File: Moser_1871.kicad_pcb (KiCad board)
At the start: 2 copper layers, 39 x 115 mm, 35 parts, among them Q14 3B SENSE / PINOUT VERIFY, SW1 SLIDE CONTACT / APPROX, U1 ATTINY461V-10SU

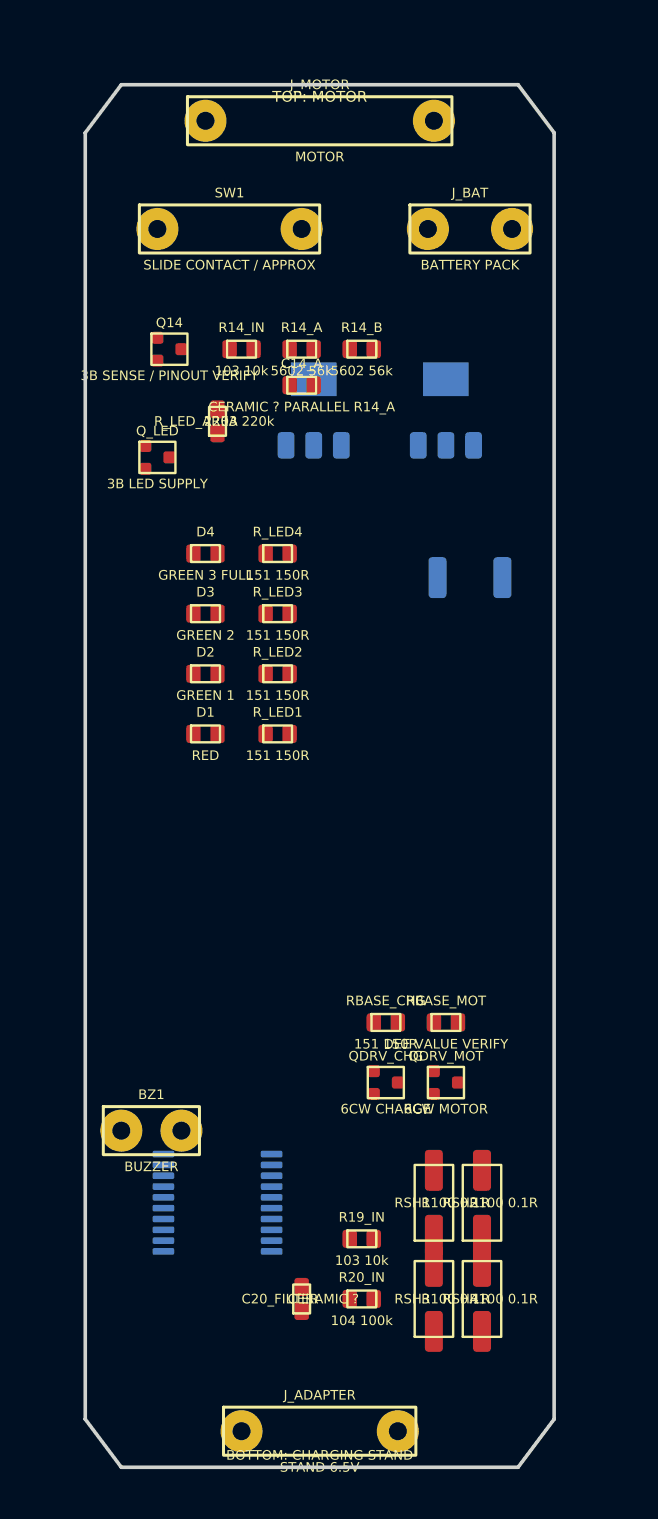
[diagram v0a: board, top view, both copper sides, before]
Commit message: Expand PCB component and via placement from board photos
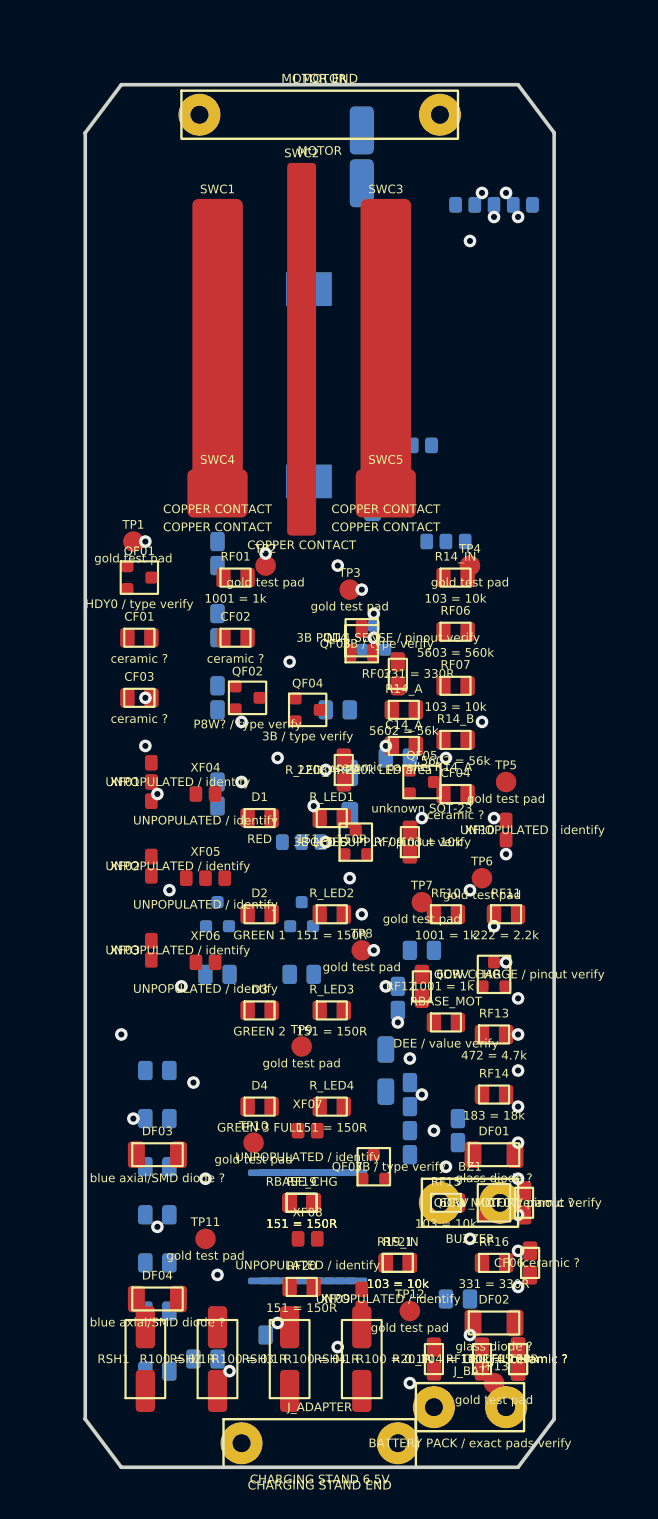
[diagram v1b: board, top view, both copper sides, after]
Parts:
- removed the D_MOTOR at (130.0, 91.0)
- removed the Q_CHG at (117.0, 77.0)
- removed the Q_MOT at (128.0, 77.0)
- removed SW1: SLIDE CONTACT / APPROX, Moser_RE:TH_2P
- added CB01: ceramic ?, Moser_RE:0805_2P, B.Cu at (104.0, 152.0)
- added CB02: ceramic ?, Moser_RE:0805_2P, B.Cu at (104.0, 148.0)
- added CB03: ceramic ?, Moser_RE:0805_2P, B.Cu at (104.0, 144.0)
- added CB04: ceramic ?, Moser_RE:0805_2P, B.Cu at (104.0, 140.0)
- added CB05: ceramic ?, Moser_RE:0805_2P, B.Cu at (104.0, 136.0)
- added CB06: ceramic ?, Moser_RE:0805_2P, B.Cu at (104.0, 132.0)
- added CB07: ceramic MCU, Moser_RE:0805_2P, B.Cu at (125.0, 138.0)
- added CB08: ceramic ?, Moser_RE:0805_2P, B.Cu at (124.0, 106.0)
- added CB09: ceramic ?, Moser_RE:0805_2P, B.Cu at (126.0, 122.0)
- added CB10: ceramic ?, Moser_RE:0805_2P, B.Cu at (129.0, 137.0)
- added CB11: ceramic ?, Moser_RE:0805_2P, B.Cu at (114.0, 154.0)
- added CF01: ceramic ?, Moser_RE:0805_2P, F.Cu at (102.5, 96.0)
- added CF02: ceramic ?, Moser_RE:0805_2P, F.Cu at (110.5, 96.0)
- added CF03: ceramic ?, Moser_RE:0805_2P, F.Cu at (102.5, 101.0)
- added CF04: ceramic ?, Moser_RE:0805_2P, F.Cu at (128.8, 109.0)
- added CF05: ceramic ?, Moser_RE:0805_2P, F.Cu at (134.0, 156.0)
- added CF06: ceramic ?, Moser_RE:0805_2P, F.Cu at (135.0, 148.0)
- added CF07: ceramic ?, Moser_RE:0805_2P, F.Cu at (134.5, 143.0)
- added DB01: glass diode ?, Moser_RE:MELF_2P, B.Cu at (120.0, 109.0)
- added DB02: small diode ?, Moser_RE:MELF_2P, B.Cu at (123.0, 132.0)
- added DF01: glass diode ?, Moser_RE:MELF_2P, F.Cu at (132.0, 139.0)
- added DF02: glass diode ?, Moser_RE:MELF_2P, F.Cu at (132.0, 153.0)
- added DF03: blue axial/SMD diode ?, Moser_RE:MELF_2P, F.Cu at (104.0, 139.0)
- added DF04: blue axial/SMD diode ?, Moser_RE:MELF_2P, F.Cu at (104.0, 151.0)
- added D_MOTOR: SS24, Moser_RE:SMB_2P, B.Cu at (121.0, 56.0)
- added QB01: 6CW / type verify, Moser_RE:SOT-23, B.Cu at (109.0, 119.0)
- added QB02: 6CW / type verify, Moser_RE:SOT-23, B.Cu at (116.0, 119.0)
- added QB03: unknown transistor/diode, Moser_RE:SOT-23, B.Cu at (122.0, 96.0)
- added QF01: HDY0 / type verify, Moser_RE:SOT-23, F.Cu at (102.5, 91.0)
- added QF02: P8W? / type verify, Moser_RE:SOT-23, F.Cu at (111.5, 101.0)
- added QF03: 3B / type verify, Moser_RE:SOT-23, F.Cu at (121.0, 96.5)
- added QF04: 3B / type verify, Moser_RE:SOT-23, F.Cu at (116.5, 102.0)
- added QF05: unknown SOT-23, Moser_RE:SOT-23, F.Cu at (126.0, 108.0)
- added QF07: 3B / type verify, Moser_RE:SOT-23, F.Cu at (122.0, 140.0)
- added Q_CHG: FZT968 CHARGE, Moser_RE:SOT-223, B.Cu at (119.0, 83.0)
- added Q_MOT: FZT968 MOTOR, Moser_RE:SOT-223, B.Cu at (119.0, 67.0)
- added RB01: 103 = 10k, Moser_RE:0805_2P, B.Cu at (104.0, 157.0)
- added RB02: 103 = 10k, Moser_RE:0805_2P, B.Cu at (108.0, 156.0)
- added RB03: 104 = 100k, Moser_RE:0805_2P, B.Cu at (125.0, 134.0)
- added RB04: 101 = 100R, Moser_RE:0805_2P, B.Cu at (129.0, 151.0)
- added RB05: 1001 = 1k, Moser_RE:0805_2P, B.Cu at (109.0, 124.0)
- added RB06: 1001 = 1k, Moser_RE:0805_2P, B.Cu at (116.0, 124.0)
- added RB07: 151 = 150R, Moser_RE:0805_2P, B.Cu at (109.0, 109.0)
- added RB08: DEE / value verify, Moser_RE:0805_2P, B.Cu at (109.0, 101.0)
- added RB09: 561 = 560R, Moser_RE:0805_2P, B.Cu at (109.0, 95.0)
- added RB10: 103 = 10k, Moser_RE:0805_2P, B.Cu at (109.0, 89.0)
- added RB11: 1001 = 1k, Moser_RE:0805_2P, B.Cu at (119.0, 102.0)
- added RB12: 1001 = 1k, Moser_RE:0805_2P, B.Cu at (124.0, 126.0)
- added RF01: 1001 = 1k, Moser_RE:0805_2P, F.Cu at (110.5, 91.0)
- added RF02: 331 = 330R, Moser_RE:0805_2P, F.Cu at (124.0, 99.0)
- added RF06: 5603 = 560k, Moser_RE:0805_2P, F.Cu at (128.8, 95.5)
- added RF07: 103 = 10k, Moser_RE:0805_2P, F.Cu at (128.8, 100.0)
- added RF09: 103 = 10k, Moser_RE:0805_2P, F.Cu at (125.0, 113.0)
- added RF10: 1001 = 1k, Moser_RE:0805_2P, F.Cu at (128.0, 119.0)
- added RF11: 222 = 2.2k, Moser_RE:0805_2P, F.Cu at (133.0, 119.0)
- added RF12: 1001 = 1k, Moser_RE:0805_2P, F.Cu at (126.0, 125.0)
- added RF13: 472 = 4.7k, Moser_RE:0805_2P, F.Cu at (132.0, 129.0)
- added RF14: 183 = 18k, Moser_RE:0805_2P, F.Cu at (132.0, 134.0)
- added RF15: 103 = 10k, Moser_RE:0805_2P, F.Cu at (128.0, 143.0)
- added RF16: 331 = 330R, Moser_RE:0805_2P, F.Cu at (132.0, 148.0)
- added RF18: 101 = 100R, Moser_RE:0805_2P, F.Cu at (131.0, 156.0)
- added RF19: 151 = 150R, Moser_RE:0805_2P, F.Cu at (116.0, 143.0)
- added RF20: 151 = 150R, Moser_RE:0805_2P, F.Cu at (116.0, 150.0)
- added RF21: 103 = 10k, Moser_RE:0805_2P, F.Cu at (124.0, 148.0)
- added SWC1: COPPER CONTACT, Moser_RE:SWITCH_CONTACT, F.Cu at (109.0, 72.0)
- added SWC2: COPPER CONTACT, Moser_RE:SWITCH_CONTACT, F.Cu at (116.0, 72.0)
- added SWC3: COPPER CONTACT, Moser_RE:SWITCH_CONTACT, F.Cu at (123.0, 72.0)
- added SWC4: COPPER CONTACT, Moser_RE:SWITCH_CONTACT, F.Cu at (109.0, 84.0)
- added SWC5: COPPER CONTACT, Moser_RE:SWITCH_CONTACT, F.Cu at (123.0, 84.0)
- added TP1: gold test pad, Moser_RE:TEST_PAD, F.Cu at (102.0, 88.0)
- added TP10: gold test pad, Moser_RE:TEST_PAD, F.Cu at (112.0, 138.0)
- added TP11: gold test pad, Moser_RE:TEST_PAD, F.Cu at (108.0, 146.0)
- added TP12: gold test pad, Moser_RE:TEST_PAD, F.Cu at (125.0, 152.0)
- added TP13: gold test pad, Moser_RE:TEST_PAD, F.Cu at (132.0, 158.0)
- added TP2: gold test pad, Moser_RE:TEST_PAD, F.Cu at (113.0, 90.0)
- added TP3: gold test pad, Moser_RE:TEST_PAD, F.Cu at (120.0, 92.0)
- added TP4: gold test pad, Moser_RE:TEST_PAD, F.Cu at (130.0, 90.0)
- added TP5: gold test pad, Moser_RE:TEST_PAD, F.Cu at (133.0, 108.0)
- added TP6: gold test pad, Moser_RE:TEST_PAD, F.Cu at (131.0, 116.0)
- added TP7: gold test pad, Moser_RE:TEST_PAD, F.Cu at (126.0, 118.0)
- added TP8: gold test pad, Moser_RE:TEST_PAD, F.Cu at (121.0, 122.0)
- added TP9: gold test pad, Moser_RE:TEST_PAD, F.Cu at (116.0, 130.0)
- added XB01: UNPOPULATED / identify, Moser_RE:UNIDENTIFIED_3P, B.Cu at (128.0, 88.0)
- added XB02: UNPOPULATED / identify, Moser_RE:UNIDENTIFIED_5P, B.Cu at (132.0, 60.0)
- added XB03: UNPOPULATED / identify, Moser_RE:UNIDENTIFIED_2P, B.Cu at (126.0, 80.0)
- added XB04: UNPOPULATED / identify, Moser_RE:UNIDENTIFIED_3P, B.Cu at (116.0, 113.0)
- added XF01: UNPOPULATED / identify, Moser_RE:UNIDENTIFIED_3P, F.Cu at (103.5, 108.0)
- added XF02: UNPOPULATED / identify, Moser_RE:UNIDENTIFIED_2P, F.Cu at (103.5, 115.0)
- added XF03: UNPOPULATED / identify, Moser_RE:UNIDENTIFIED_2P, F.Cu at (103.5, 122.0)
- added XF04: UNPOPULATED / identify, Moser_RE:UNIDENTIFIED_2P, F.Cu at (108.0, 109.0)
- added XF05: UNPOPULATED / identify, Moser_RE:UNIDENTIFIED_3P, F.Cu at (108.0, 116.0)
- added XF06: UNPOPULATED / identify, Moser_RE:UNIDENTIFIED_2P, F.Cu at (108.0, 123.0)
- added XF07: UNPOPULATED / identify, Moser_RE:UNIDENTIFIED_2P, F.Cu at (116.5, 137.0)
- added XF08: UNPOPULATED / identify, Moser_RE:UNIDENTIFIED_2P, F.Cu at (116.5, 146.0)
- added XF09: UNPOPULATED / identify, Moser_RE:UNIDENTIFIED_2P, F.Cu at (121.0, 151.0)
- added XF10: UNPOPULATED / identify, Moser_RE:UNIDENTIFIED_2P, F.Cu at (133.0, 112.0)
- C14_A: value CERAMIC ? PARALLEL R14_A -> ceramic parallel R14_A
- C20_FILTER: value CERAMIC ? -> ceramic ?
- J_ADAPTER: value STAND 6.5V -> CHARGING STAND 6.5V
- J_BAT: value BATTERY PACK -> BATTERY PACK / exact pads verify
- Q14: value 3B SENSE / PINOUT VERIFY -> 3B PIN14 SENSE / pinout verify
- QDRV_CHG: value 6CW CHARGE -> 6CW CHARGE / pinout verify
- QDRV_MOT: value 6CW MOTOR -> 6CW MOTOR / pinout verify
- Q_LED: value 3B LED SUPPLY -> 3B LED SUPPLY / pinout verify
- R14_A, R14_B: value 5602 56k -> 5602 = 56k
- R14_IN, R19_IN: value 103 10k -> 103 = 10k
- R20_IN: value 104 100k -> 104 = 100k
- RBASE_CHG, R_LED1, R_LED2, R_LED3, R_LED4: value 151 150R -> 151 = 150R
- RBASE_MOT: value DEE VALUE VERIFY -> DEE / value verify
- RSH1, RSH2, RSH3, RSH4: value R100 0.1R -> R100 = 0.1R
- R_LED_AREA: value 2203 220k -> 2203 = 220k LED area
- moved J_BAT 98.0 mm to (130.0, 160.0)
- moved D4 46.2 mm to (112.5, 135.0)
- moved R_LED4 46.2 mm to (118.5, 135.0)
- moved Q_LED 36.0 mm to (120.5, 113.0), turned to 90 degrees
- moved R14_B 33.4 mm to (128.8, 104.5)
- moved D3 33.3 mm to (112.5, 127.0)
- moved R_LED3 33.3 mm to (118.5, 127.0)
- moved C14_A 31.2 mm to (124.5, 105.0)
- moved R14_A 31.2 mm to (124.5, 102.0)
- moved R_LED_AREA 30.8 mm to (119.5, 107.0)
- moved Q14 28.8 mm to (121.0, 96.0), turned to 90 degrees
- moved RSH1 27.3 mm to (103.0, 156.0)
- moved BZ1 27.2 mm to (130.0, 143.0)
- moved R14_IN 26.0 mm to (128.8, 91.0)
- moved RSH2 25.6 mm to (109.0, 156.0)
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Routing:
- net (no net): vias 0 -> 63
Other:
- board text added: "B.Cu: MCU, buzzer, FZT968, SS24 and driver network"
- board text added: "CHARGING STAND END"
- board text added: "F.Cu: LEDs, switch contacts, shunts and dense small-signal network"
- board text added: "MOSER 1871 PCB PHOTO MAP v0.4 - APPROXIMATE / NOT FOR MANUFACTURE"
- board text added: "MOTOR END"
- board text added: "No copper tracks reconstructed yet; component/via placement stage only"
- board text added: "Universal footprints and values marked ? must be verified under microscope"
- board text removed: "B.Cu side: ATtiny, buzzer, FZT968 and SS24"
- board text removed: "BOTTOM: CHARGING STAND"
- board text removed: "Board outline and coordinates are approximate - measure real PCB before fabrication"
- board text removed: "F.Cu side: LEDs, shunts, switch contacts and small passives"
- board text removed: "MOSER 1871 REVERSE ENGINEERING - APPROXIMATE PLACEMENT / NOT FOR MANUFACTURE"
- board text removed: "TOP: MOTOR"

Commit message: Make external solder pads independently movable
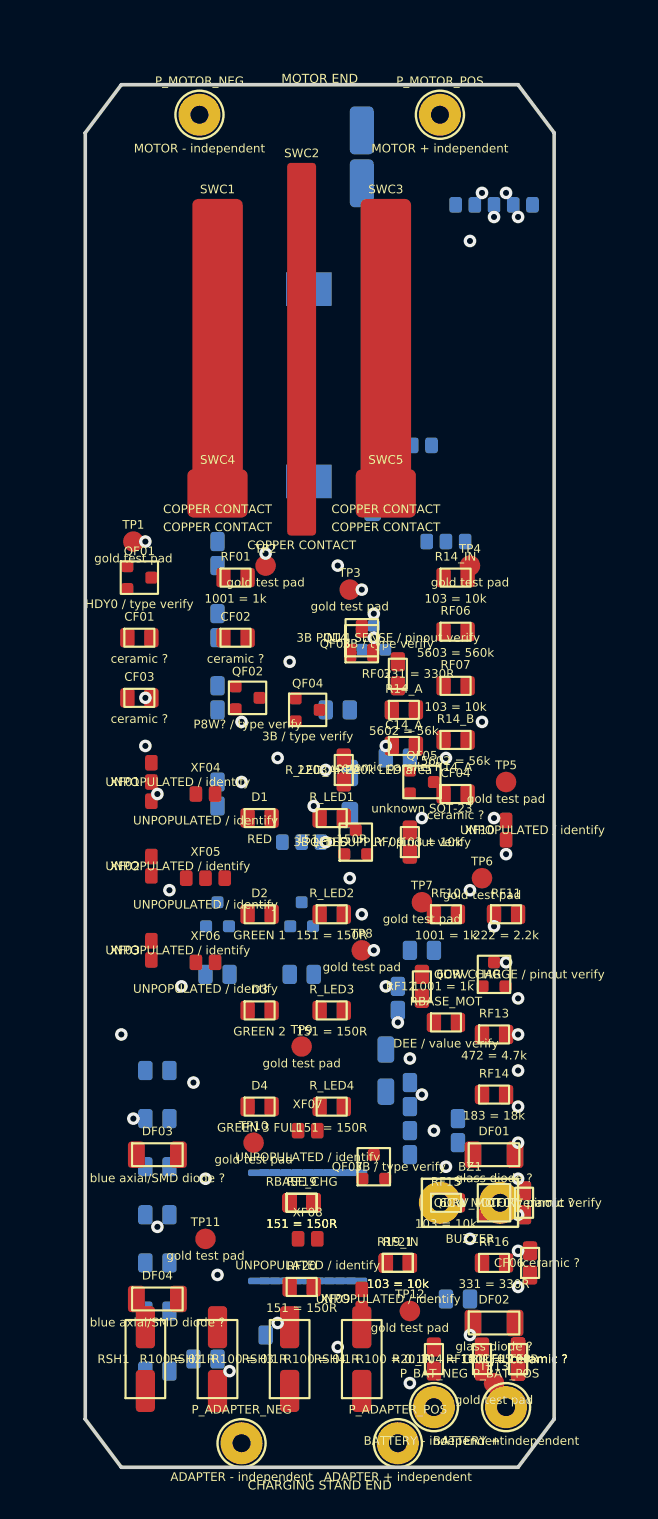
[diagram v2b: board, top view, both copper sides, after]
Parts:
- removed J_ADAPTER: CHARGING STAND 6.5V, Moser_RE:TH_2P
- removed J_BAT: BATTERY PACK / exact pads verify, Moser_RE:TH_2P
- removed J_MOTOR: MOTOR, Moser_RE:TH_2P
- added P_ADAPTER_NEG: ADAPTER - independent, Moser_RE:TH_SINGLE_PAD, F.Cu at (111.0, 163.0)
- added P_ADAPTER_POS: ADAPTER + independent, Moser_RE:TH_SINGLE_PAD, F.Cu at (124.0, 163.0)
- added P_BAT_NEG: BATTERY - independent, Moser_RE:TH_SINGLE_PAD, F.Cu at (127.0, 160.0)
- added P_BAT_POS: BATTERY + independent, Moser_RE:TH_SINGLE_PAD, F.Cu at (133.0, 160.0)
- added P_MOTOR_NEG: MOTOR - independent, Moser_RE:TH_SINGLE_PAD, F.Cu at (107.5, 52.5)
- added P_MOTOR_POS: MOTOR + independent, Moser_RE:TH_SINGLE_PAD, F.Cu at (127.5, 52.5)
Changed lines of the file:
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@@
 	(gr_line (start 98 161) (end 98 54) (stroke (width 0.3) (type default)) (layer "Edge.Cuts"))
 	(gr_line (start 98 54) (end 101 50) (stroke (width 0.3) (type default)) (layer "Edge.Cuts"))
-	(footprint "Moser_RE:TH_2P"
+	(footprint "Moser_RE:TH_SINGLE_PAD"
 		(layer "F.Cu")
-		(at 117.5 52.5)
-		(property "Reference" "J_MOTOR"
-			(at 0 -3 0)
+		(at 107.5 52.5)
+		(property "Reference" "P_MOTOR_NEG"
+			(at 0 -2.8 0)
 			(layer "F.SilkS")
 			(effects (font (size 0.72 0.72) (thickness 0.11)))
 		)
-		(property "Value" "MOTOR"
-			(at 0 3 0)
+		(property "Value" "MOTOR - independent"
+			(at 0 2.8 0)
 			(layer "F.SilkS")
 			(effects (font (size 0.72 0.72) (thickness 0.11)))
 		)
-		(fp_rect (start -11.5 -2) (end 11.5 2) (stroke (width 0.2) (type default)) (fill none) (layer "F.SilkS"))
-		(pad "1" thru_hole circle (at -10.0 0) (size 3.5 3.5) (drill 1.5) (layers "*.Cu" "*.Mask")
+		(fp_circle (center 0 0) (end 2 0) (stroke (width 0.2) (type default)) (fill none) (layer "F.SilkS"))
+		(pad "1" thru_hole circle (at 0 0) (size 3.5 3.5) (drill 1.5) (layers "*.Cu" "*.Mask")
 			(net 7 "MOTOR-"))
-		(pad "2" thru_hole circle (at 10.0 0) (size 3.5 3.5) (drill 1.5) (layers "*.Cu" "*.Mask")
-			(net 6 "MOTOR+"))
 	)
-	(footprint "Moser_RE:TH_2P"
+	(footprint "Moser_RE:TH_SINGLE_PAD"
 		(layer "F.Cu")
-		(at 117.5 163)
-		(property "Reference" "J_ADAPTER"
-			(at 0 -3 0)
+		(at 127.5 52.5)
+		(property "Reference" "P_MOTOR_POS"
+			(at 0 -2.8 0)
 			(layer "F.SilkS")
 			(effects (font (size 0.72 0.72) (thickness 0.11)))
 		)
-		(property "Value" "CHARGING STAND 6.5V"
-			(at 0 3 0)
+		(property "Value" "MOTOR + independent"
+			(at 0 2.8 0)
 			(layer "F.SilkS")
 			(effects (font (size 0.72 0.72) (thickness 0.11)))
 		)
-		(fp_rect (start -8.0 -2) (end 8.0 2) (stroke (width 0.2) (type default)) (fill none) (layer "F.SilkS"))
-		(pad "1" thru_hole circle (at -6.5 0) (size 3.5 3.5) (drill 1.5) (layers "*.Cu" "*.Mask")
-			(net 5 "ADAPTER-"))
-		(pad "2" thru_hole circle (at 6.5 0) (size 3.5 3.5) (drill 1.5) (layers "*.Cu" "*.Mask")
-			(net 4 "ADAPTER+"))
+		(fp_circle (center 0 0) (end 2 0) (stroke (width 0.2) (type default)) (fill none) (layer "F.SilkS"))
+		(pad "1" thru_hole circle (at 0 0) (size 3.5 3.5) (drill 1.5) (layers "*.Cu" "*.Mask")
+			(net 6 "MOTOR+"))
 	)
-	(footprint "Moser_RE:TH_2P"
+	(footprint "Moser_RE:TH_SINGLE_PAD"
 		(layer "F.Cu")
-		(at 130 160)
-		(property "Reference" "J_BAT"
-			(at 0 -3 0)
+		(at 111 163)
+		(property "Reference" "P_ADAPTER_NEG"
+			(at 0 -2.8 0)
 			(layer "F.SilkS")
 			(effects (font (size 0.72 0.72) (thickness 0.11)))
 		)
-		(property "Value" "BATTERY PACK / exact pads verify"
-			(at 0 3 0)
+		(property "Value" "ADAPTER - independent"
+			(at 0 2.8 0)
 			(layer "F.SilkS")
 			(effects (font (size 0.72 0.72) (thickness 0.11)))
 		)
-		(fp_rect (start -4.5 -2) (end 4.5 2) (stroke (width 0.2) (type default)) (fill none) (layer "F.SilkS"))
-		(pad "1" thru_hole circle (at -3.0 0) (size 3.5 3.5) (drill 1.5) (layers "*.Cu" "*.Mask")
+		(fp_circle (center 0 0) (end 2 0) (stroke (width 0.2) (type default)) (fill none) (layer "F.SilkS"))
+		(pad "1" thru_hole circle (at 0 0) (size 3.5 3.5) (drill 1.5) (layers "*.Cu" "*.Mask")
+			(net 5 "ADAPTER-"))
+	)
+	(footprint "Moser_RE:TH_SINGLE_PAD"
+		(layer "F.Cu")
+		(at 124 163)
+		(property "Reference" "P_ADAPTER_POS"
+			(at 0 -2.8 0)
+			(layer "F.SilkS")
+			(effects (font (size 0.72 0.72) (thickness 0.11)))
+		)
+		(property "Value" "ADAPTER + independent"
+			(at 0 2.8 0)
+			(layer "F.SilkS")
+			(effects (font (size 0.72 0.72) (thickness 0.11)))
+		)
+		(fp_circle (center 0 0) (end 2 0) (stroke (width 0.2) (type default)) (fill none) (layer "F.SilkS"))
+		(pad "1" thru_hole circle (at 0 0) (size 3.5 3.5) (drill 1.5) (layers "*.Cu" "*.Mask")
+			(net 4 "ADAPTER+"))
+	)
+	(footprint "Moser_RE:TH_SINGLE_PAD"
+		(layer "F.Cu")
+		(at 127 160)
+		(property "Reference" "P_BAT_NEG"
+			(at 0 -2.8 0)
+			(layer "F.SilkS")
+			(effects (font (size 0.72 0.72) (thickness 0.11)))
+		)
+		(property "Value" "BATTERY - independent"
+			(at 0 2.8 0)
+			(layer "F.SilkS")
+			(effects (font (size 0.72 0.72) (thickness 0.11)))
+		)
+		(fp_circle (center 0 0) (end 2 0) (stroke (width 0.2) (type default)) (fill none) (layer "F.SilkS"))
+		(pad "1" thru_hole circle (at 0 0) (size 3.5 3.5) (drill 1.5) (layers "*.Cu" "*.Mask")
 			(net 3 "BAT-"))
-		(pad "2" thru_hole circle (at 3.0 0) (size 3.5 3.5) (drill 1.5) (layers "*.Cu" "*.Mask")
+	)
+	(footprint "Moser_RE:TH_SINGLE_PAD"
+		(layer "F.Cu")
+		(at 133 160)
+		(property "Reference" "P_BAT_POS"
+			(at 0 -2.8 0)
+			(layer "F.SilkS")
+			(effects (font (size 0.72 0.72) (thickness 0.11)))
+		)
+		(property "Value" "BATTERY + independent"
+			(at 0 2.8 0)
+			(layer "F.SilkS")
+			(effects (font (size 0.72 0.72) (thickness 0.11)))
+		)
+		(fp_circle (center 0 0) (end 2 0) (stroke (width 0.2) (type default)) (fill none) (layer "F.SilkS"))
+		(pad "1" thru_hole circle (at 0 0) (size 3.5 3.5) (drill 1.5) (layers "*.Cu" "*.Mask")
 			(net 2 "BAT+"))
 	)

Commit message: Correct ATtiny461 orientation from backside view
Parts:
- turned U1 to 180 degrees
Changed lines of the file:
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@@
 	(footprint "Moser_RE:SOIC-20"
 		(layer "B.Cu")
-		(at 116.5 145 90)
+		(at 116.5 145 180)
 		(property "Reference" "U1"
 			(at 0 -6.2 0)

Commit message: Preserve manual placement and correct ATtiny backside pin orientation
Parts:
- moved P_MOTOR_POS 8.50 mm to (135.0, 48.5)
- moved P_MOTOR_NEG 8.39 mm to (100.0, 48.8)
- moved U1 4.70 mm to (114.5, 140.8)
- moved D_MOTOR 3.40 mm to (118.7, 53.5), turned to 0 degrees
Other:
- board size 39 x 115 mm -> 39 x 119 mm
